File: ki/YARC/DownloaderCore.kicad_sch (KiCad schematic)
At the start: 13 parts, among them J1 NANOIO_EXT, J2 MCR_EXT, J3 PULSE_EXT, U1 74HCT574, U2 74HCT574, U3 74HCT574, U4 74HCT574, U5 74HCT574, U6 74LS138, U7 74HCT574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

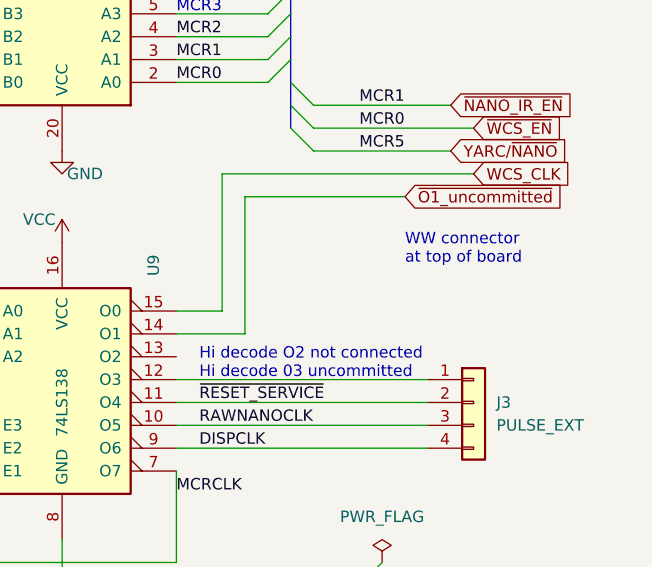
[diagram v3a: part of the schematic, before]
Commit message: ALU schematic checking complete. Ready to start layout.
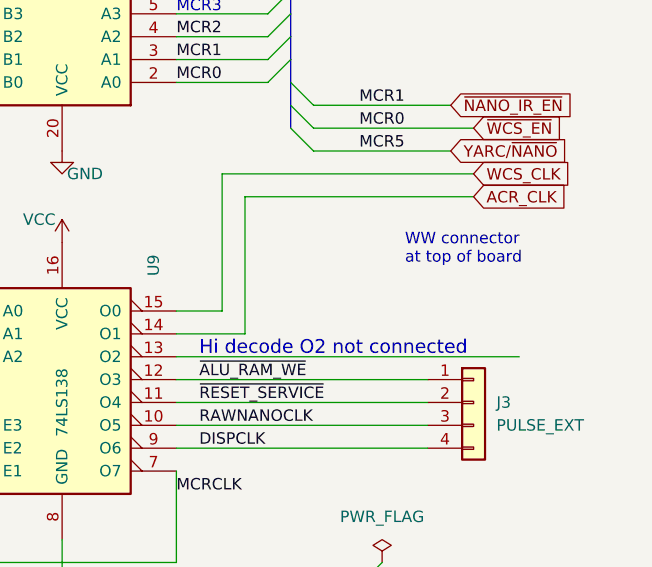
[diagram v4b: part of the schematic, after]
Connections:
- net ~{ALU_RAM_WE}: now reaches J3.1 (Pin_1), U9.12 (O3)
- net ~{O1_uncommitted} renamed ACR_CLK
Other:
- note added: "Hi decode O2 not connected"
- note removed: "Hi decode O2 not connected Hi decode 03 uncommitted"
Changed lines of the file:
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@@
+    (stroke (width 0) (type default) (color 0 0 0 0))
+  )
+  (wire (pts (xy 218.44 134.62) (xy 256.54 134.62))
     (stroke (width 0) (type default) (color 0 0 0 0))
   )
@@
     (stroke (width 0) (type default) (color 0 0 0 0))
   )
-  (wire (pts (xy 243.84 116.84) (xy 226.06 116.84))
+  (wire (pts (xy 251.46 116.84) (xy 226.06 116.84))
     (stroke (width 0) (type default) (color 0 0 0 0))
   )
@@
     (effects (font (size 1.27 1.27)) (justify left bottom))
   )
-  (text "Hi decode O2 not connected\nHi decode 03 uncommitted"
-    (at 220.98 137.16 0)
-    (effects (font (size 1.27 1.27)) (justify left bottom))
+  (text "Hi decode O2 not connected" (at 220.98 134.62 0)
+    (effects (font (size 1.524 1.524)) (justify left bottom))
   )
   (text "MCR5 YARC/NANO#" (at 233.68 87.63 0)
@@
   (label "MCR4" (at 246.38 60.96 180)
     (effects (font (size 1.27 1.27)) (justify right bottom))
+  )
+  (label "~{ALU_RAM_WE}" (at 220.98 137.16 0)
+    (effects (font (size 1.27 1.27)) (justify left bottom))
   )
   (label "NANOIO1" (at 144.78 60.96 90)
@@
     )
   )
-  (global_label "~{O1_uncommitted}" (shape input) (at 243.84 116.84 0) (fields_autoplaced)
+  (global_label "ACR_CLK" (shape input) (at 251.46 116.84 0) (fields_autoplaced)
     (effects (font (size 1.27 1.27)) (justify left))
-    (property "Intersheet References" "${INTERSHEET_REFS}" (id 0) (at 261.9769 116.7606 0)
+    (property "Intersheet References" "${INTERSHEET_REFS}" (id 0) (at 262.0374 116.7606 0)
       (effects (font (size 1.27 1.27)) (justify left) hide)
     )

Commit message: Continuing corrections (only - no new functionality)
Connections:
- net ~{ALU_RAM_WE} renamed Not connected
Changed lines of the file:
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@@
     (effects (font (size 1.27 1.27)) (justify right bottom))
-  )
-  (label "~{ALU_RAM_WE}" (at 220.98 137.16 0)
-    (effects (font (size 1.27 1.27)) (justify left bottom))
   )
   (label "NANOIO1" (at 144.78 60.96 90)
@@
     (effects (font (size 1.27 1.27)) (justify left bottom))
   )
+  (label "Not connected" (at 220.98 137.16 0)
+    (effects (font (size 1.27 1.27)) (justify left bottom))
+  )

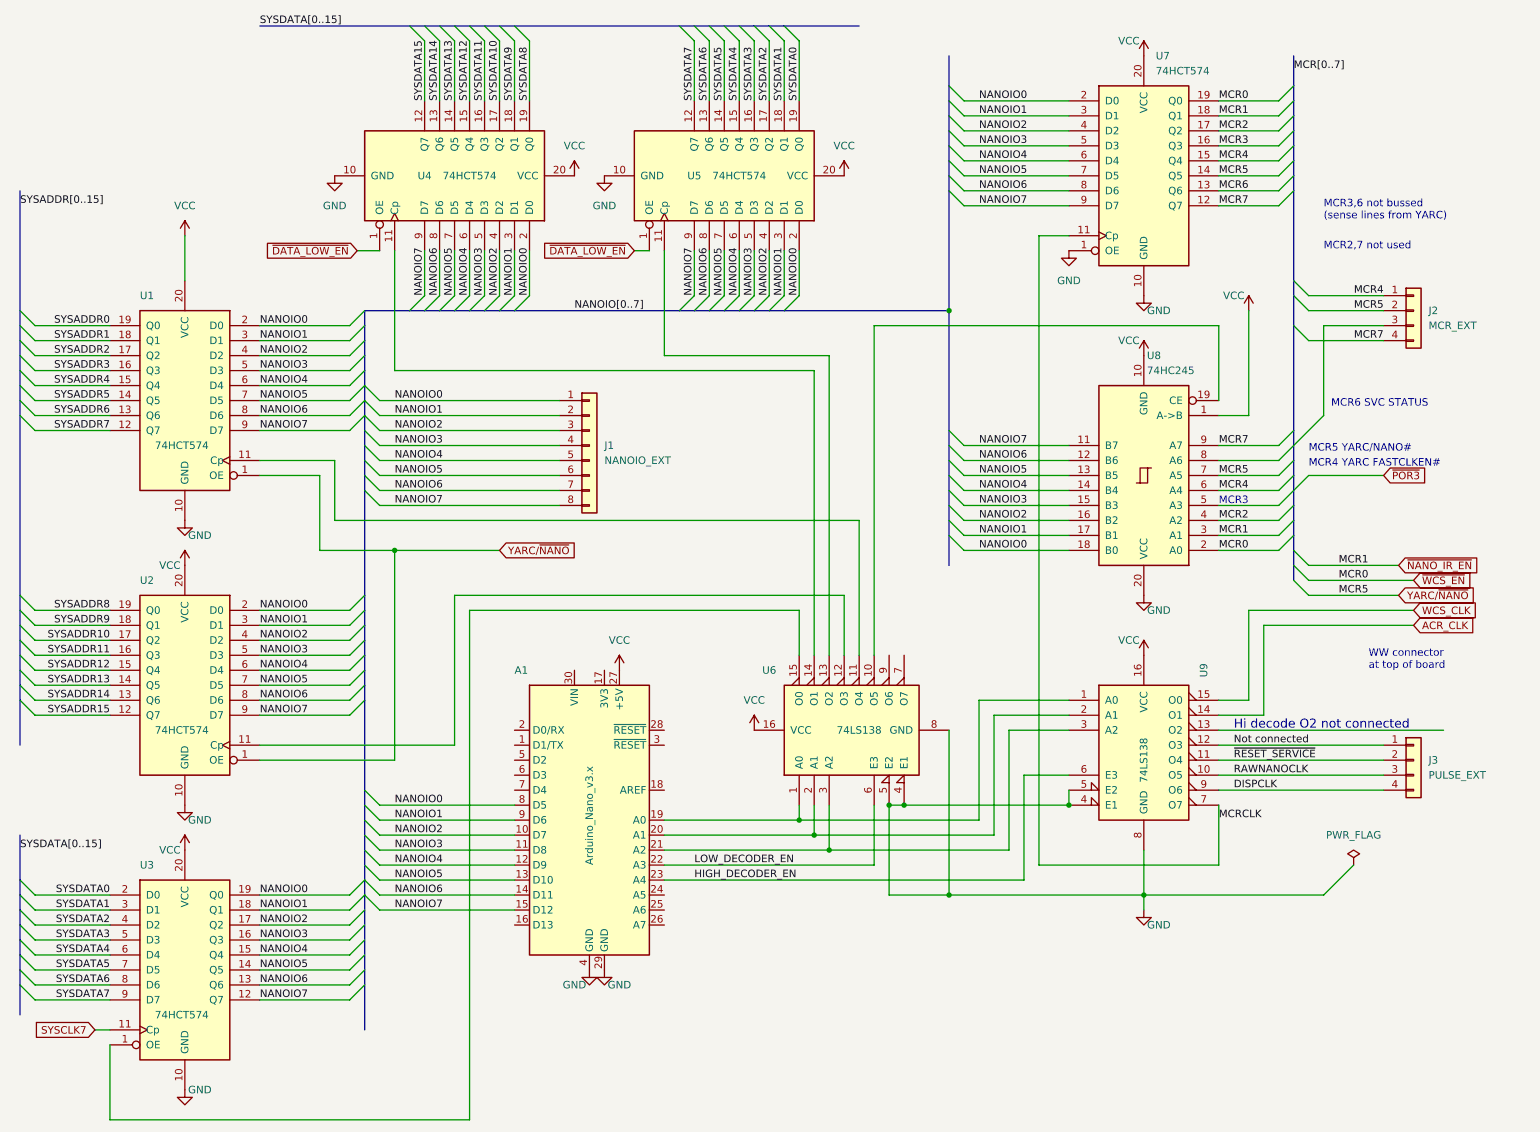
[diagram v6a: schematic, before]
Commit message: Removed about 2/3 of 2300+ errors from the ERC
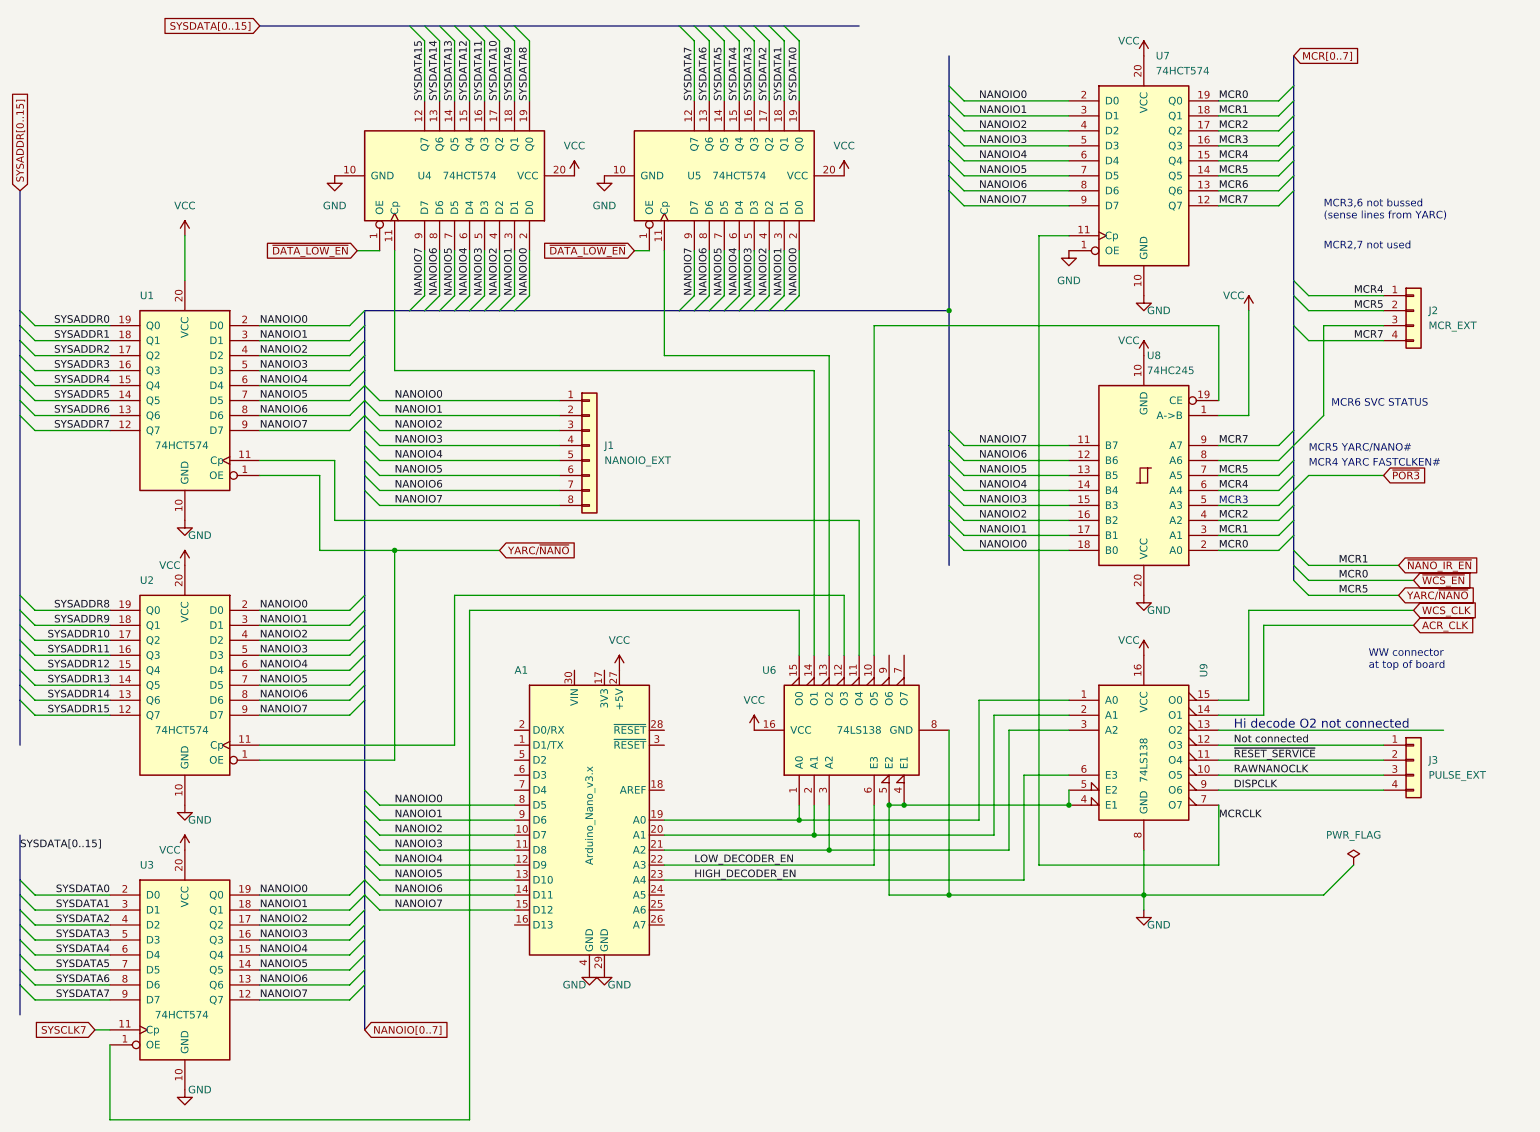
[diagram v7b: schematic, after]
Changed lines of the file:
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@@
-    (effects (font (size 1.27 1.27)) (justify left bottom))
-  )
-  (label "SYSADDR[0..15]" (at 15.24 45.72 0) (fields_autoplaced)
     (effects (font (size 1.27 1.27)) (justify left bottom))
   )
@@
     (effects (font (size 1.27 1.27)) (justify left bottom))
   )
-  (label "NANOIO[0..7]" (at 109.22 63.5 0) (fields_autoplaced)
-    (effects (font (size 1.27 1.27)) (justify left bottom))
-  )
   (label "LOW_DECODER_EN" (at 129.54 157.48 0) (fields_autoplaced)
     (effects (font (size 1.27 1.27)) (justify left bottom))
@@
     (effects (font (size 1.27 1.27)) (justify left bottom))
   )
-  (label "SYSDATA[0..15]" (at 55.88 15.24 0) (fields_autoplaced)
-    (effects (font (size 1.27 1.27)) (justify left bottom))
-  )
   (label "SYSDATA12" (at 91.44 27.94 90) (fields_autoplaced)
     (effects (font (size 1.27 1.27)) (justify left bottom))
@@
     (effects (font (size 1.27 1.27)) (justify left bottom))
   )
-  (label "MCR[0..7]" (at 231.14 22.86 0) (fields_autoplaced)
-    (effects (font (size 1.27 1.27)) (justify left bottom))
-  )
   (label "SYSDATA0" (at 30.48 162.56 180) (fields_autoplaced)
     (effects (font (size 1.27 1.27)) (justify right bottom))
@@
     (effects (font (size 1.27 1.27)) (justify left))
     (property "Intersheetrefs" "${INTERSHEET_REFS}" (at 262.0374 116.7606 0)
+      (effects (font (size 1.27 1.27)) (justify left) hide)
+    )
+  )
+  (global_label "SYSADDR[0..15]" (shape input) (at 15.24 43.18 90) (fields_autoplaced)
+    (effects (font (size 1.27 1.27)) (justify left))
+    (property "Intersheetrefs" "${INTERSHEET_REFS}" (at 15.24 25.2571 90)
+      (effects (font (size 1.27 1.27)) (justify left) hide)
+    )
+  )
+  (global_label "NANOIO[0..7]" (shape input) (at 73.66 185.42 0) (fields_autoplaced)
+    (effects (font (size 1.27 1.27)) (justify left))
+    (property "Intersheetrefs" "${INTERSHEET_REFS}" (at 88.9826 185.42 0)
       (effects (font (size 1.27 1.27)) (justify left) hide)
     )
@@
     )
   )
+  (global_label "SYSDATA[0..15]" (shape input) (at 55.88 15.24 180) (fields_autoplaced)
+    (effects (font (size 1.27 1.27)) (justify right))
+    (property "Intersheetrefs" "${INTERSHEET_REFS}" (at 38.4409 15.24 0)
+      (effects (font (size 1.27 1.27)) (justify right) hide)
+    )
+  )
+  (global_label "MCR[0..7]" (shape input) (at 231.14 20.32 0) (fields_autoplaced)
+    (effects (font (size 1.27 1.27)) (justify left))
+    (property "Intersheetrefs" "${INTERSHEET_REFS}" (at 243.4386 20.32 0)
+      (effects (font (size 1.27 1.27)) (justify left) hide)
+    )
+  )

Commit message: Ongoing fixes for ERC errors
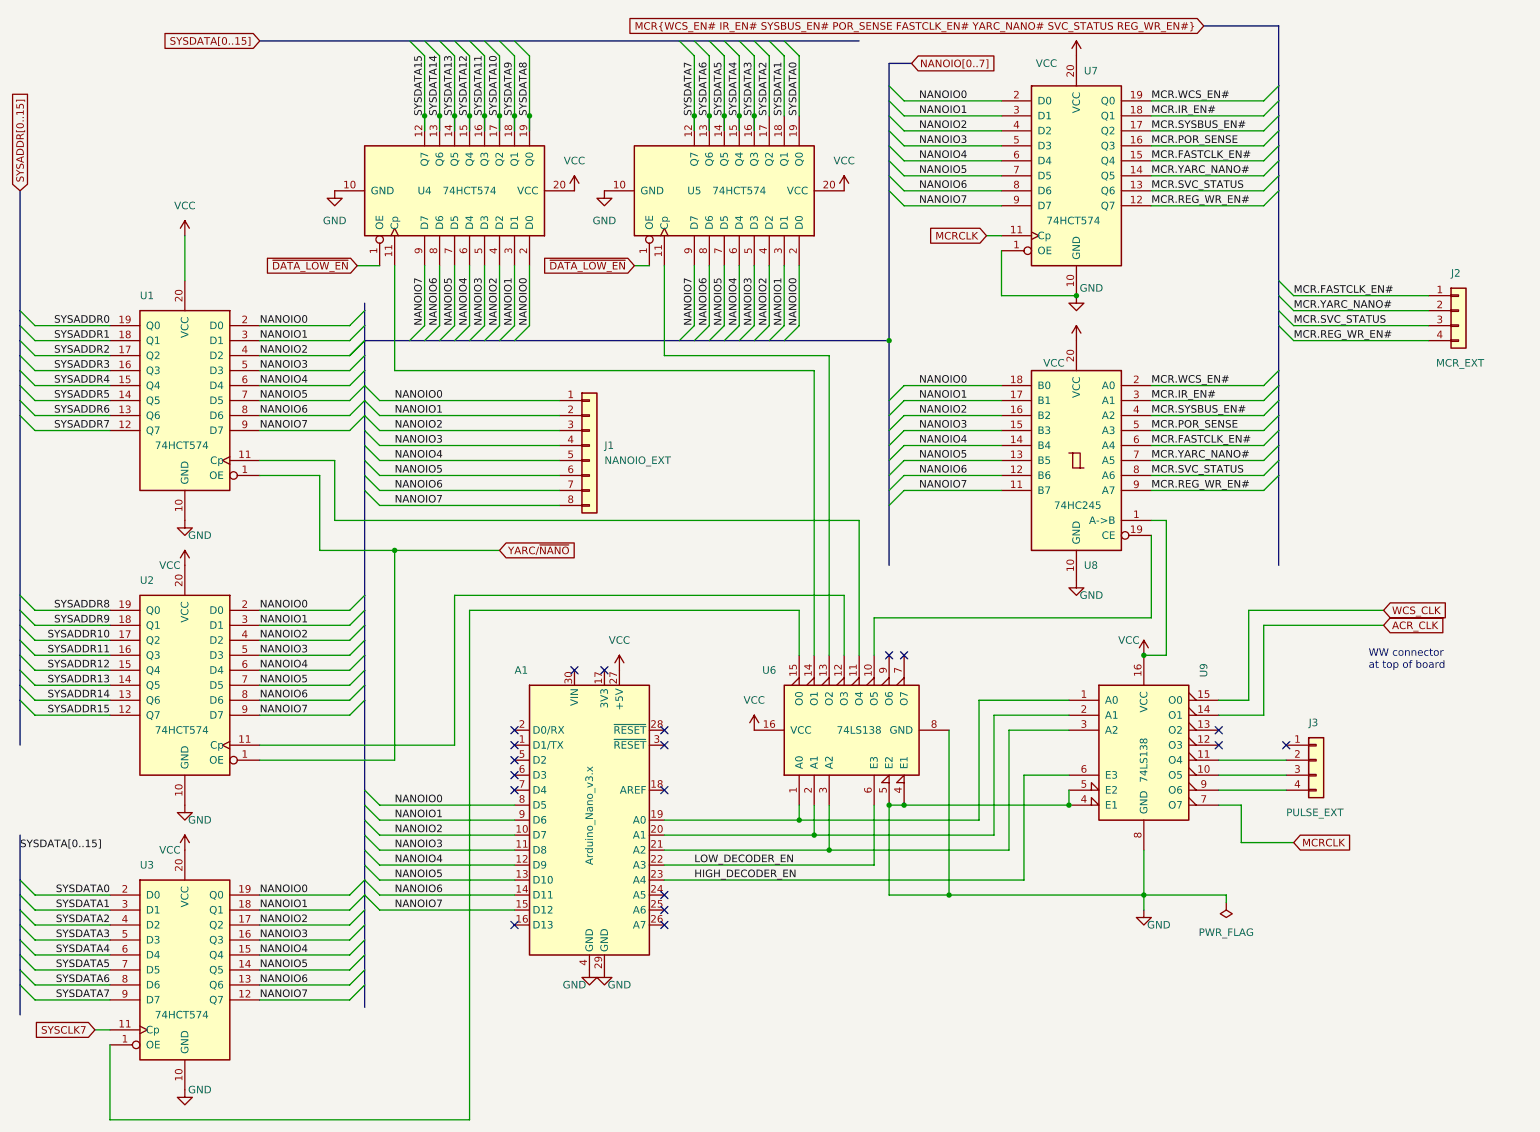
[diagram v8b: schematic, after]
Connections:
- net MCR6 is gone; now on net MCR.SVC_STATUS: U7.13 (Q6)
- net ~{POR3} is gone; now on net MCR.POR_SENSE: U8.5 (A3)
- net GND: now also U8.10 (GND); no longer U8.20 (VCC)
- net VCC: now also U8.20 (VCC); no longer U8.10 (GND)
- net YARC/~{NANO}: no longer J2.2 (Pin_2), U7.14 (Q5), U8.7 (A5)
- net MCR.SVC_STATUS: now reaches J2.3 (Pin_3), U8.8 (A6)
- net DISPCLK: no longer names the net of J3.4 (Pin_4), U9.9 (O6)
- net MCR2 renamed MCR.SYSBUS_EN#
- net MCR3 renamed MCR.POR_SENSE
- net MCR4 renamed MCR.FASTCLK_EN#
- net MCR7 renamed MCR.REG_WR_EN#
- net Not connected: no longer names the net of J3.1 (Pin_1)
- net Not connected: no longer U9.12 (O3)
- net RAWNANOCLK: no longer names the net of J3.3 (Pin_3), U9.10 (O5)
- net ~{NANO_IR_EN} renamed MCR.IR_EN#
- net ~{RESET_SERVICE}: no longer names the net of J3.2 (Pin_2), U9.11 (O4)
- net ~{WCS_EN} renamed MCR.WCS_EN#
- new net MCR.YARC_NANO#: J2.2 (Pin_2), U7.14 (Q5), U8.7 (A5)
- no-connect marks 0 -> 19
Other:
- note removed: "Hi decode O2 not connected"
- note removed: "MCR2,7 not used"
- note removed: "MCR3"
- note removed: "MCR3,6 not bussed (sense lines from YARC)"
- note removed: "MCR4 YARC FASTCLKEN#"
- note removed: "MCR5 YARC/NANO#"
- note removed: "MCR6 SVC STATUS"
- moved on the sheet: J2, J3, U4, U5, U7, U8
